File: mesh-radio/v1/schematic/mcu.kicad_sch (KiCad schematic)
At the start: 34 parts, among them U8 NRF52840-QIAA-F-R7, Y1 32MHz, Y2 32.768kHz

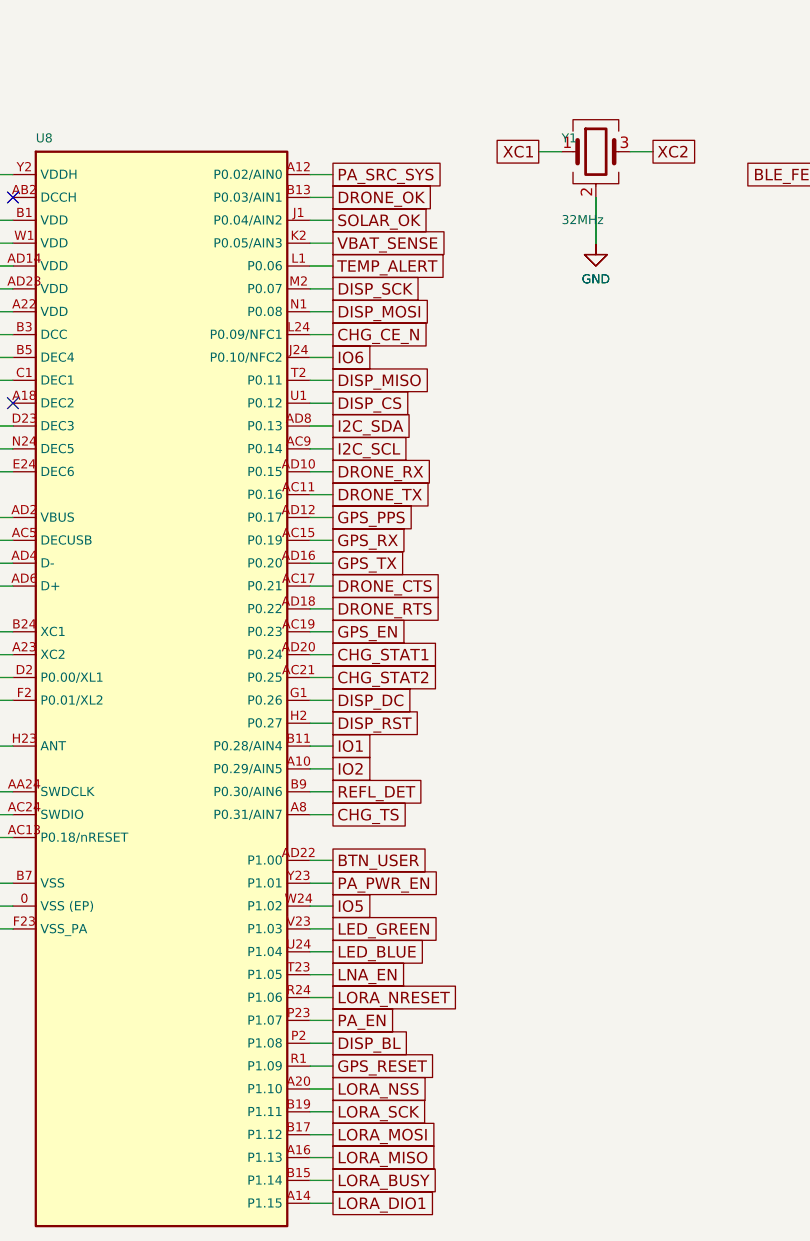
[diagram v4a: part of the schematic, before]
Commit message: Mesh Radio v1: ratio detector circuit and RF re-run in progress (snapshot)
Co-Authored-By: Claude Opus 5.5 <noreply@anthropic.com>
Claude-Session: https://claude.ai/code/session_015TBB2ThqxHSgA8MkFosmn9
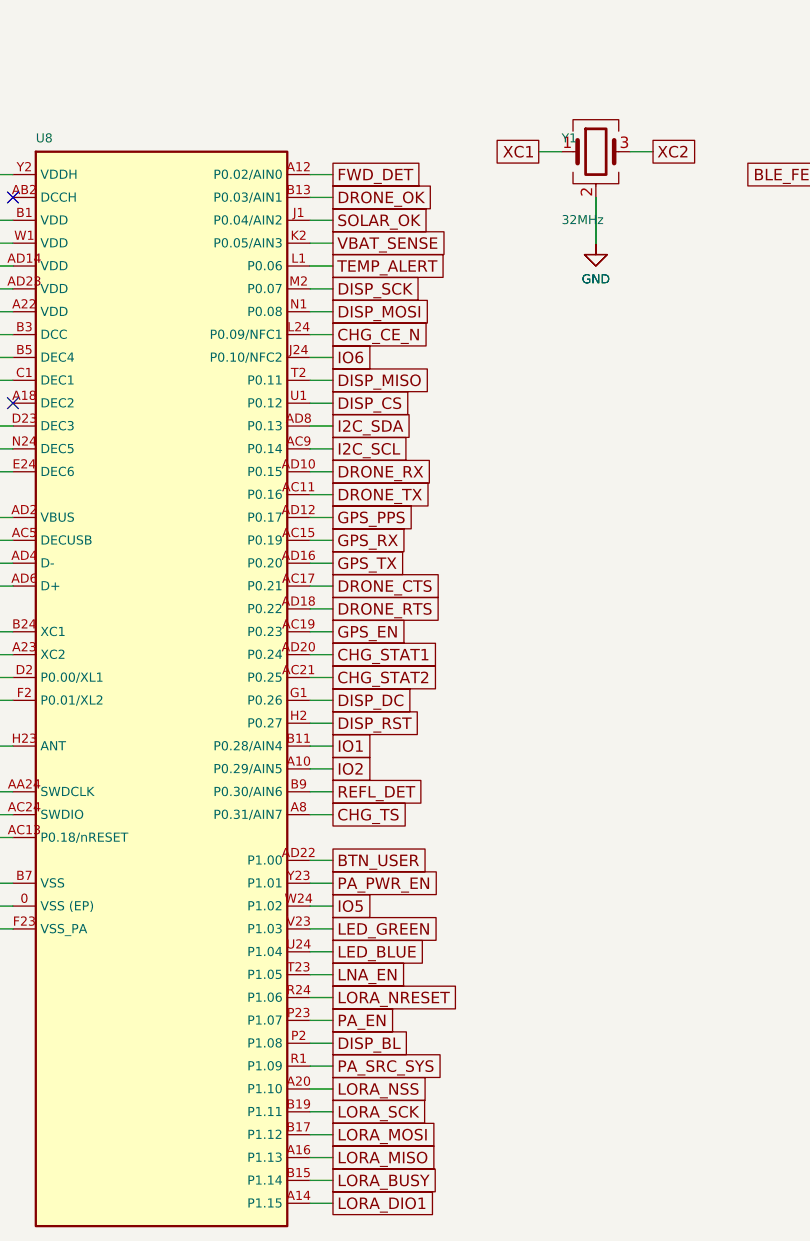
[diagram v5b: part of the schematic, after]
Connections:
- net GPS_RESET is gone; now on net PA_SRC_SYS: U8.R1 (P1.09)
- net PA_SRC_SYS: no longer U8.A12 (P0.02/AIN0)
- new net FWD_DET: U8.A12 (P0.02/AIN0)
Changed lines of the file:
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@@
 		)
 	)
-	(global_label "PA_SRC_SYS"
+	(global_label "FWD_DET"
 		(shape passive)
 		(at 74.93 48.26 0)
@@
 		)
 	)
-	(global_label "GPS_RESET"
+	(global_label "PA_SRC_SYS"
 		(shape passive)
 		(at 74.93 147.32 0)
